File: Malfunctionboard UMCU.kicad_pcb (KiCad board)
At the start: 2 copper layers, 214 parts, among them J101 Conn_02x05_Odd_Even, J102 Conn_02x05_Odd_Even, J201 Conn_Coaxial, J202 Conn_Coaxial, J301 Conn_Coaxial, J302 Conn_Coaxial, J401 Conn_Coaxial, J402 Conn_Coaxial, J501 Conn_Coaxial, J502 Conn_Coaxial, J601 Conn_Coaxial, J602 Conn_Coaxial, J701 Conn_Coaxial, J702 Conn_Coaxial, J801 Conn_Coaxial, J802 Conn_Coaxial, J901 Conn_Coaxial, J902 Conn_Coaxial, Q101 NTR5103NT1G, Q102 RSC002P03T316, Q103 RSC002P03T316, Q104 NTR5103NT1G, Q201 NTR5103NT1G, Q202 NTR5103NT1G, Q301 NTR5103NT1G, Q302 NTR5103NT1G, Q401 NTR5103NT1G, Q402 NTR5103NT1G, Q501 NTR5103NT1G, Q502 NTR5103NT1G, Q601 NTR5103NT1G, Q602 NTR5103NT1G, Q701 NTR5103NT1G, Q702 NTR5103NT1G, Q801 NTR5103NT1G, Q802 NTR5103NT1G, Q901 NTR5103NT1G, Q902 NTR5103NT1G, U201 Opamp_Quad_Generic, U301 Opamp_Quad_Generic, U401 Opamp_Quad_Generic, U501 Opamp_Quad_Generic, U601 Opamp_Quad_Generic, U701 Opamp_Quad_Generic, U801 Opamp_Quad_Generic, U901 Opamp_Quad_Generic

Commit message: Made first pcb sketch, but is too wide
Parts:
- added J201: Conn_Coaxial, _Custom:Solder straight thin coax cable, F.Cu at (155.5, 185.1)
- added J201: Conn_Coaxial, _Custom:Solder straight thin coax cable, F.Cu at (89.5, 185.1)
- added J201: Conn_Coaxial, _Custom:Solder straight thin coax cable, F.Cu at (82.2, 185.1)
- added J201: Conn_Coaxial, _Custom:Solder straight thin coax cable, F.Cu at (74.9, 185.1)
- added J201: Conn_Coaxial, _Custom:Solder straight thin coax cable, F.Cu at (67.5, 185.1)
- added J201: Conn_Coaxial, _Custom:Solder straight thin coax cable, F.Cu at (60.2, 185.1)
- added J201: Conn_Coaxial, _Custom:Solder straight thin coax cable, F.Cu at (52.9, 185.1)
- added J201: Conn_Coaxial, _Custom:Solder straight thin coax cable, F.Cu at (45.5, 185.1)
- added J201: Conn_Coaxial, _Custom:Solder straight thin coax cable, F.Cu at (148.2, 185.1)
- added J201: Conn_Coaxial, _Custom:Solder straight thin coax cable, F.Cu at (140.8, 185.1)
- added J201: Conn_Coaxial, _Custom:Solder straight thin coax cable, F.Cu at (133.5, 185.1)
- added J201: Conn_Coaxial, _Custom:Solder straight thin coax cable, F.Cu at (126.2, 185.1)
- added J201: Conn_Coaxial, _Custom:Solder straight thin coax cable, F.Cu at (118.8, 185.1)
- added J201: Conn_Coaxial, _Custom:Solder straight thin coax cable, F.Cu at (111.5, 185.1)
- added J201: Conn_Coaxial, _Custom:Solder straight thin coax cable, F.Cu at (104.2, 185.1)
- added J201: Conn_Coaxial, _Custom:Solder straight thin coax cable, F.Cu at (96.9, 185.1)
- moved C203 272.1 mm to (89.2, 108.2), turned to 270 degrees
- moved R202 265.1 mm to (92.7, 105.0), turned to 270 degrees
- moved C204 263.4 mm to (89.2, 112.3), turned to 270 degrees
- moved R204 255.5 mm to (102.9, 124.0), turned to 90 degrees
- moved Q201 254.7 mm to (102.1, 115.6), turned to 270 degrees
- moved R205 253.8 mm to (97.5, 120.9), turned to 180 degrees
- moved R203 253.5 mm to (102.1, 120.9)
- moved Q202 252.7 mm to (97.5, 115.6), turned to 270 degrees
- moved L203 252.4 mm to (92.7, 111.3), turned to 90 degrees
- moved C201 251.3 mm to (110.5, 108.2), turned to 270 degrees
- moved L204 251.2 mm to (92.7, 118.9), turned to 90 degrees
- moved D201 250.9 mm to (102.9, 127.8), turned to 90 degrees
- moved R206 250.2 mm to (96.8, 124.0), turned to 90 degrees
- moved D202 249.6 mm to (96.8, 127.8), turned to 90 degrees
- moved C205 249.1 mm to (98.8, 118.6)
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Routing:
- net /Ref+: track 0.00 -> 45.7 mm, vias 0 -> 5
- net +12V: track 0.00 -> 44.2 mm, vias 0 -> 5
- net -5V: track 0.00 -> 41.9 mm, vias 0 -> 3
- net /Ref-: track 0.00 -> 40.5 mm, vias 0 -> 2
- net /sheet5DD8DCB3/LED_GND: track 0.00 -> 29.8 mm, vias 0 -> 2
- net Net-(D202-Pad1): track 0.00 -> 26.0 mm
- net Net-(D201-Pad1): track 0.00 -> 25.2 mm
- net Net-(C201-Pad2): track 0.00 -> 14.6 mm
- net /V_in: track 0.00 -> 14.2 mm
- net Net-(C203-Pad2): track 0.00 -> 14.2 mm
- net /sheet5DF3552C/Malf: track 0.00 -> 11.9 mm, vias 0 -> 1
- net /sheet5DF3552B/Malf: track 0.00 -> 11.9 mm, vias 0 -> 1
- net Net-(C204-Pad2): track 0.00 -> 6.98 mm
- net Net-(C202-Pad2): track 0.00 -> 6.98 mm
- net Net-(J202-Pad1): track 0.00 -> 6.50 mm
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- added copper zone on B.Cu, net GND
- added copper zone on F.Cu, net GND
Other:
- net class Default: via_dia 0.8 -> 0.6; via_drill 0.4 -> 0.25
- rule via_min_drill: 0.3 -> 0.25
- board text added: "Should be this far apart"

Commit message: Finished main pcb design. Todo: move decouple C's to backside, move logic at connectors to back, better mounting hole position
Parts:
- removed the C203 at (89.2, 108.2)
- removed the J201 at (155.5, 185.1)
- removed the J201 at (89.5, 185.1)
- removed the J201 at (82.2, 185.1)
- removed the J201 at (74.9, 185.1)
- removed the J201 at (67.5, 185.1)
- removed the J201 at (60.2, 185.1)
- removed the J201 at (52.9, 185.1)
- removed the J201 at (45.5, 185.1)
- removed the J201 at (106.9, 133.9)
- removed the J201 at (148.2, 185.1)
- removed the J201 at (140.8, 185.1)
- removed the J201 at (133.5, 185.1)
- removed the J201 at (126.2, 185.1)
- removed the J201 at (118.8, 185.1)
- removed the J201 at (111.5, 185.1)
- removed the J201 at (104.2, 185.1)
- removed the J201 at (96.9, 185.1)
- removed JP101, JP102: Jumper, Connector_PinHeader_2.54mm:PinHeader_1x02_P2.54mm_Vertical
- removed the R103 at (347.1, 40.5)
- removed the R201 at (106.9, 105.0)
- removed the R204 at (102.9, 124.0)
- added C204: 10n, Capacitor_SMD:C_0805_2012Metric, F.Cu at (103.6, 108.2)
- added D108: 5.4V, Diode_SMD:D_SOD-323, F.Cu at (81.8, 121.9)
- added D109: 12V, Diode_SMD:D_SOD-323, F.Cu at (86.4, 116.8)
- added H1: MH_Pad, MountingHole:MountingHole_3.2mm_M3, F.Cu at (88.6, 122.3)
- added H10: MH_Pad, MountingHole:MountingHole_3.2mm_M3, F.Cu at (148.1, 123.3)
- added H2: MH_Pad, MountingHole:MountingHole_3.2mm_M3, F.Cu at (88.6, 109.3)
- added H3: MH_Pad, MountingHole:MountingHole_3.2mm_M3, F.Cu at (208.5, 132.5)
- added H4: MH_Pad, MountingHole:MountingHole_3.2mm_M3, F.Cu at (68.0, 103.1)
- added H5: MH_Pad, MountingHole:MountingHole_3.2mm_M3, F.Cu at (208.3, 103.1)
- added H6: MH_Pad, MountingHole:MountingHole_3.2mm_M3, F.Cu at (68.0, 132.5)
- added H7: MH_Pad, MountingHole:MountingHole_3.2mm_M3, F.Cu at (71.9, 121.8)
- added H7: MH_Pad, MountingHole:MountingHole_3.2mm_M3, F.Cu at (71.9, 113.5)
- added H8: MH_Pad, MountingHole:MountingHole_3.2mm_M3, F.Cu at (177.6, 123.3)
- added H9: MH_Pad, MountingHole:MountingHole_3.2mm_M3, F.Cu at (118.4, 123.3)
- added J201: Conn_Coaxial, _Custom:Solder straight thin coax cable, F.Cu at (92.6, 129.9)
- added R101: 10k, Resistor_SMD:R_0805_2012Metric, F.Cu at (71.8, 115.4)
- added R203: 10k, Resistor_SMD:R_0805_2012Metric, B.Cu at (87.9, 130.7)
- added R205: 150R, Resistor_SMD:R_0805_2012Metric, F.Cu at (99.9, 105.5)
- C203: renamed from C205; moved to B.Cu
- C303: renamed from C305; moved to B.Cu
- C403: renamed from C405; moved to B.Cu
- C503: renamed from C505; moved to B.Cu
- C603: renamed from C605; moved to B.Cu
- C703: renamed from C705; moved to B.Cu
- C803: renamed from C805; moved to B.Cu
- C903: renamed from C905; moved to B.Cu
- D101, D107: value 15V -> 5.4V
- D103: value 5V -> 15V
- D104: value 12V -> 5V
- D105, D106: value 5.4V -> 15V
- Q101: value NTR5103NT1G -> RSC002P03T316
- Q103: value RSC002P03T316 -> NTR5103NT1G
- Q201, Q202, Q301, Q302, Q401, Q402, Q501, Q502, Q601, Q602, Q701, Q702, Q801, Q802, Q901, Q902, R206, R306, R406, R506, R606, R706, R806, R906, U201, U301, U401, U501, U601, U701, U801, U901: moved to B.Cu
- R102: value 10k -> 100k
- R201: renamed from R203; moved to B.Cu
- R204: renamed from R205; moved to B.Cu
- R301: renamed from R303; moved to B.Cu
- R303: renamed from R304; moved to B.Cu
- R304: renamed from R305; moved to B.Cu
- R401: renamed from R403; moved to B.Cu
- R403: renamed from R404; moved to B.Cu
- R404: renamed from R405; moved to B.Cu
- R501: renamed from R503; moved to B.Cu
- R503: renamed from R504; moved to B.Cu
- R504: renamed from R505; moved to B.Cu
- R601: renamed from R603; moved to B.Cu
- R603: renamed from R604; moved to B.Cu
- R604: renamed from R605; moved to B.Cu
- R701: renamed from R703; moved to B.Cu
- R703: renamed from R704; moved to B.Cu
- R704: renamed from R705; moved to B.Cu
- R801: renamed from R803; moved to B.Cu
- R803: renamed from R804; moved to B.Cu
- R804: renamed from R805; moved to B.Cu
- R901: renamed from R903; moved to B.Cu
- R903: renamed from R904; moved to B.Cu
- R904: renamed from R905; moved to B.Cu
- moved R303 317.3 mm to (102.7, 130.7), turned to 180 degrees
- moved D301 316.8 mm to (103.7, 131.6), turned to 90 degrees
- moved R302 312.7 mm to (107.4, 105.5), turned to 270 degrees
- moved C302 309.2 mm to (103.7, 114.7)
- moved Q302 307.4 mm to (113.3, 116.5), turned to 270 degrees
- moved R503 306.9 mm to (132.3, 130.7), turned to 180 degrees
- moved L301 306.6 mm to (107.4, 111.3), turned to 90 degrees
- moved R304 305.7 mm to (113.3, 121.8)
- moved R306 305.5 mm to (110.1, 130.7), turned to 180 degrees
- moved C303 305.4 mm to (112.1, 119.5), turned to 180 degrees
- moved R305 305.1 mm to (114.7, 105.5), turned to 270 degrees
- moved C501 304.1 mm to (133.3, 110.2)
- moved Q301 304.0 mm to (108.8, 116.5), turned to 270 degrees
- moved C301 303.5 mm to (103.7, 110.2)
- moved C305 303.4 mm to (118.4, 112.6), turned to 180 degrees
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- renumbered C103 to C102, C105 to C103, C107 to C104, C109 to C105, C111 to C106, C113 to C107, C115 to C108, C117 to C109, C119 to C110, C102 to C111, C104 to C112, C106 to C113, C108 to C114, C110 to C115, C112 to C116, C114 to C117, C116 to C118, C118 to C119, C204 to C205, C303 to C304, C304 to C305, C403 to C404, C404 to C405, C503 to C504, C504 to C505, C603 to C604, C604 to C605, C703 to C704, C704 to C705, C803 to C804, C804 to C805, C903 to C904, C904 to C905, R101 to R103, R301 to R302, R302 to R305, R401 to R402, R402 to R405, R501 to R502, R502 to R505, R601 to R602, R602 to R605, R701 to R702, R702 to R705, R801 to R802, R802 to R805, R901 to R902, R902 to R905
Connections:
- D101 pad 1: /Malf -> GND
- D101 pad 2: GND -> -5V
- D102 pad 1: Net-(D102-Pad1) -> +12V
- D103 pad 2: /V_in -> GND
- D104 pad 1: Net-(D103-Pad1) -> Net-(D104-Pad1)
- D104 pad 2: GND -> /V_in
- D105 pad 1: GND -> /Malf
- D105 pad 2: /Ref- -> GND
- D106 pad 1: GND -> Net-(D106-Pad1)
- D106 pad 2: /Ref+ -> GND
- D107 pad 1: Net-(D107-Pad1) -> GND
- D107 pad 2: GND -> /Ref-
- J101 pad 8: Net-(D102-Pad1) -> Net-(D106-Pad1)
- J102 pad 8: Net-(D107-Pad1) -> Net-(D103-Pad1)
- L203 pad 2: Net-(C203-Pad2) -> Net-(C204-Pad2)
- Q101 pad 1: /V_in -> /sheet5DD8DCB3/Malf_in
- Q101 pad 2: GND -> Net-(D106-Pad1)
- Q102 pad 2: Net-(D102-Pad1) -> Net-(D103-Pad1)
- Q102 pad 3: Net-(Q102-Pad3) -> Net-(Q101-Pad3)
- Q103 pad 1: /sheet5DD8DCB3/Malf_in -> Net-(Q103-Pad1)
- Q103 pad 2: Net-(D107-Pad1) -> GND
- Q103 pad 3: Net-(Q102-Pad3) -> /sheet5DD8DCB3/LED_GND
- Q104 pad 1: Net-(Q101-Pad3) -> /V_in
- Q104 pad 3: /sheet5DD8DCB3/LED_GND -> Net-(Q103-Pad1)
- Q201 pad 3: /sheet5DF3552B/Malf -> /sheet5DD8DCB3/Malf_in
- Q202 pad 2: /sheet5DF3552C/Malf -> /sheet5DD8DCB3/Malf
- Q301 pad 3: /sheet5DF270F1/Malf -> /sheet5DD8DCB3/Malf
- Q302 pad 2: /sheet5DF3552B/Malf -> /sheet5DE59C6C/Malf
- Q401 pad 3: /sheet5DF270F0/Malf -> /sheet5DE59C6C/Malf
- Q402 pad 2: /sheet5DF270F1/Malf -> /sheet5DF0CFC9/Malf
- Q501 pad 3: /sheet5DF0CFCA/Malf -> /sheet5DF0CFC9/Malf
- Q502 pad 2: /sheet5DF270F0/Malf -> /sheet5DF0CFCA/Malf
- Q601 pad 3: /sheet5DF0CFC9/Malf -> /sheet5DF0CFCA/Malf
- Q602 pad 2: /sheet5DF0CFCA/Malf -> /sheet5DF270F0/Malf
- Q701 pad 3: /sheet5DE59C6C/Malf -> /sheet5DF270F0/Malf
- Q702 pad 2: /sheet5DF0CFC9/Malf -> /sheet5DF270F1/Malf
- Q801 pad 3: /sheet5DD8DCB3/Malf -> /sheet5DF270F1/Malf
- Q802 pad 2: /sheet5DE59C6C/Malf -> /sheet5DF3552B/Malf
- Q901 pad 3: /sheet5DD8DCB3/Malf_in -> /sheet5DF3552B/Malf
- Q902 pad 2: /sheet5DD8DCB3/Malf -> /sheet5DF3552C/Malf
- R102 pad 2: /sheet5DD8DCB3/Malf_in -> Net-(Q103-Pad1)
- R202 pad 2: Net-(C203-Pad2) -> Net-(C201-Pad2)
- U201 pad 12: Net-(C203-Pad2) -> Net-(C204-Pad2)
- U201 pad 9: Net-(C203-Pad2) -> Net-(C204-Pad2)
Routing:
- net +12V: track 44.2 -> 363.9 mm, vias 5 -> 32
- net /Ref-: track 40.5 -> 277.8 mm, vias 2 -> 16
- net /Ref+: track 45.7 -> 261.3 mm, vias 5 -> 34
- net -5V: track 41.9 -> 209.5 mm, vias 3 -> 18
- net /V_in: track 14.2 -> 174.2 mm, vias 0 -> 3
- net /sheet5DD8DCB3/LED_GND: track 29.8 -> 182.1 mm, vias 2 -> 1
- net Net-(D801-Pad1): track 0.00 -> 31.7 mm, vias 0 -> 3
- net Net-(D501-Pad1): track 0.00 -> 31.7 mm, vias 0 -> 3
- net Net-(D901-Pad1): track 0.00 -> 31.7 mm, vias 0 -> 3
- net Net-(D601-Pad1): track 0.00 -> 31.7 mm, vias 0 -> 3
- net Net-(D301-Pad1): track 0.00 -> 31.7 mm, vias 0 -> 3
- net Net-(D401-Pad1): track 0.00 -> 31.7 mm, vias 0 -> 3
- net Net-(D701-Pad1): track 0.00 -> 31.7 mm, vias 0 -> 3
- net Net-(D902-Pad1): track 0.00 -> 31.4 mm, vias 0 -> 3
- net Net-(D702-Pad1): track 0.00 -> 31.4 mm, vias 0 -> 3
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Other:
- board outline added: 144.9 x 33.7 mm
- board text added: "Ch1"
- board text removed: "Should be this far apart"

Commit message: Finished v0.1
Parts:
- removed C101, C102, C103, C104, C105, C106, C107, C108, C109, C110, C111, C112, C113, C114, C115, C116, C117, C118, C119, C120: 10n, Capacitor_SMD:C_0805_2012Metric
- removed the D104 at (85.1, 119.6)
- removed the D105 at (74.2, 121.9)
- removed the D107 at (82.3, 118.5)
- removed H2, H4, H6, H7 (x2), H8, H9: MH_Pad, MountingHole:MountingHole_3.2mm_M3
- removed the Q104 at (79.2, 117.9)
- removed the R303 at (102.7, 130.7)
- removed the R403 at (117.5, 130.7)
- removed the R503 at (132.3, 130.7)
- removed the R603 at (147.1, 130.7)
- removed the R703 at (161.9, 130.7)
- removed the R803 at (176.7, 130.7)
- removed the R903 at (191.5, 130.7)
- added C201: 10n, Capacitor_SMD:C_0805_2012Metric, F.Cu at (88.8, 106.7)
- added C206: 10n, Capacitor_SMD:C_0805_2012Metric, B.Cu at (102.6, 105.3)
- added C207: 10n, Capacitor_SMD:C_0805_2012Metric, B.Cu at (91.8, 103.1)
- added C208: 10n, Capacitor_SMD:C_0805_2012Metric, B.Cu at (103.6, 108.5)
- added C209: 10n, Capacitor_SMD:C_0805_2012Metric, B.Cu at (97.2, 104.6)
- added C210: 10n, Capacitor_SMD:C_0805_2012Metric, B.Cu at (91.0, 119.0)
- added C212: 10n, Capacitor_SMD:C_0805_2012Metric, B.Cu at (93.5, 130.3)
- added C303: 10n, Capacitor_SMD:C_0805_2012Metric, B.Cu at (104.9, 114.8)
- added C306: 10n, Capacitor_SMD:C_0805_2012Metric, B.Cu at (117.4, 105.3)
- added C307: 10n, Capacitor_SMD:C_0805_2012Metric, B.Cu at (108.4, 104.6)
- added C308: 10n, Capacitor_SMD:C_0805_2012Metric, B.Cu at (118.4, 108.5)
- added C309: 10n, Capacitor_SMD:C_0805_2012Metric, B.Cu at (112.0, 104.6)
- added C310: 10n, Capacitor_SMD:C_0805_2012Metric, B.Cu at (103.7, 118.6)
- added C312: 10n, Capacitor_SMD:C_0805_2012Metric, B.Cu at (108.3, 130.3)
- added C403: 10n, Capacitor_SMD:C_0805_2012Metric, B.Cu at (119.7, 114.8)
- added C406: 10n, Capacitor_SMD:C_0805_2012Metric, B.Cu at (132.2, 105.3)
- added C407: 10n, Capacitor_SMD:C_0805_2012Metric, B.Cu at (123.2, 104.6)
- added C408: 10n, Capacitor_SMD:C_0805_2012Metric, B.Cu at (133.2, 108.5)
- added C409: 10n, Capacitor_SMD:C_0805_2012Metric, B.Cu at (126.8, 104.6)
- added C410: 10n, Capacitor_SMD:C_0805_2012Metric, B.Cu at (118.5, 118.6)
- added C412: 10n, Capacitor_SMD:C_0805_2012Metric, B.Cu at (123.1, 130.3)
- added C503: 10n, Capacitor_SMD:C_0805_2012Metric, B.Cu at (134.5, 114.8)
- added C506: 10n, Capacitor_SMD:C_0805_2012Metric, B.Cu at (147.0, 105.3)
- added C507: 10n, Capacitor_SMD:C_0805_2012Metric, B.Cu at (138.0, 104.6)
- added C508: 10n, Capacitor_SMD:C_0805_2012Metric, B.Cu at (148.0, 108.5)
- added C509: 10n, Capacitor_SMD:C_0805_2012Metric, B.Cu at (141.6, 104.6)
- added C510: 10n, Capacitor_SMD:C_0805_2012Metric, B.Cu at (133.3, 118.6)
- added C512: 10n, Capacitor_SMD:C_0805_2012Metric, B.Cu at (137.9, 130.3)
- added C603: 10n, Capacitor_SMD:C_0805_2012Metric, B.Cu at (149.3, 114.8)
- added C606: 10n, Capacitor_SMD:C_0805_2012Metric, B.Cu at (161.8, 105.3)
- added C607: 10n, Capacitor_SMD:C_0805_2012Metric, B.Cu at (152.8, 104.6)
- added C608: 10n, Capacitor_SMD:C_0805_2012Metric, B.Cu at (162.8, 108.5)
- added C609: 10n, Capacitor_SMD:C_0805_2012Metric, B.Cu at (156.4, 104.6)
- added C610: 10n, Capacitor_SMD:C_0805_2012Metric, B.Cu at (148.1, 118.6)
- added C612: 10n, Capacitor_SMD:C_0805_2012Metric, B.Cu at (152.7, 130.3)
- added C703: 10n, Capacitor_SMD:C_0805_2012Metric, B.Cu at (164.1, 114.8)
- added C706: 10n, Capacitor_SMD:C_0805_2012Metric, B.Cu at (176.6, 105.3)
- added C707: 10n, Capacitor_SMD:C_0805_2012Metric, B.Cu at (167.6, 104.6)
- added C708: 10n, Capacitor_SMD:C_0805_2012Metric, B.Cu at (177.6, 108.5)
- added C709: 10n, Capacitor_SMD:C_0805_2012Metric, B.Cu at (171.2, 104.6)
- added C710: 10n, Capacitor_SMD:C_0805_2012Metric, B.Cu at (162.9, 118.6)
- added C712: 10n, Capacitor_SMD:C_0805_2012Metric, B.Cu at (167.5, 130.3)
- added C803: 10n, Capacitor_SMD:C_0805_2012Metric, B.Cu at (178.9, 114.8)
- added C806: 10n, Capacitor_SMD:C_0805_2012Metric, B.Cu at (191.4, 105.3)
- added C807: 10n, Capacitor_SMD:C_0805_2012Metric, B.Cu at (182.4, 104.6)
- added C808: 10n, Capacitor_SMD:C_0805_2012Metric, B.Cu at (192.4, 108.4)
- added C809: 10n, Capacitor_SMD:C_0805_2012Metric, B.Cu at (186.0, 104.6)
- added C810: 10n, Capacitor_SMD:C_0805_2012Metric, B.Cu at (177.7, 118.6)
- added C812: 10n, Capacitor_SMD:C_0805_2012Metric, B.Cu at (182.3, 130.3)
- added C903: 10n, Capacitor_SMD:C_0805_2012Metric, B.Cu at (193.7, 114.8)
- added C906: 10n, Capacitor_SMD:C_0805_2012Metric, B.Cu at (205.0, 105.9)
- added C907: 10n, Capacitor_SMD:C_0805_2012Metric, B.Cu at (197.2, 104.6)
- added C908: 10n, Capacitor_SMD:C_0805_2012Metric, B.Cu at (205.7, 108.0)
- added C909: 10n, Capacitor_SMD:C_0805_2012Metric, B.Cu at (200.8, 104.6)
- added C910: 10n, Capacitor_SMD:C_0805_2012Metric, B.Cu at (192.5, 118.6)
- added C912: 10n, Capacitor_SMD:C_0805_2012Metric, B.Cu at (197.1, 130.3)
- added D101: 15V, Diode_SMD:D_SOD-323, F.Cu at (76.5, 120.4)
- added D103: 5V, Diode_SMD:D_SOD-323, F.Cu at (81.9, 115.8)
- added D106: 5.4V, Diode_SMD:D_SOD-323, F.Cu at (80.4, 120.4)
- added H101: MH_Pad, MountingHole:MountingHole_3.2mm_M3, F.Cu at (86.9, 117.9)
- added H107: MH_Pad, MountingHole:MountingHole_3.2mm_M3, F.Cu at (85.9, 103.1)
- added H108: MH_Pad, MountingHole:MountingHole_3.2mm_M3, F.Cu at (85.6, 131.6)
- added Q103: RSC002P03T316, Package_TO_SOT_SMD:SOT-23, B.Cu at (79.1, 117.9)
- added R304: 10k, Resistor_SMD:R_0805_2012Metric, B.Cu at (104.7, 132.6)
- added R404: 10k, Resistor_SMD:R_0805_2012Metric, B.Cu at (119.4, 132.6)
- added R504: 10k, Resistor_SMD:R_0805_2012Metric, B.Cu at (134.2, 132.6)
- added R604: 10k, Resistor_SMD:R_0805_2012Metric, B.Cu at (149.0, 132.6)
- added R704: 10k, Resistor_SMD:R_0805_2012Metric, B.Cu at (163.8, 132.6)
- added R804: 10k, Resistor_SMD:R_0805_2012Metric, B.Cu at (178.6, 132.6)
- added R904: 10k, Resistor_SMD:R_0805_2012Metric, B.Cu at (193.4, 132.6)
- added SYM101: SYM_Magnet_Small, _Custom:UMC_logo_small, B.Cu at (114.0, 125.6)
- C202: renamed from C201; moved to B.Cu
- C203: renamed from C202; moved to B.Cu
- C204, C205, C302, C304, C305, C402, C404, C405, C502, C504, C505, C602, C604, C605, C702, C704, C705, C802, C804, C805, C902, C904, C905, Q102: moved to B.Cu
- D102: renamed from D106; moved to B.Cu
- D109: renamed from D103; moved to B.Cu
- Q101: value RSC002P03T316 -> NTR5103NT1G; moved to B.Cu
- Q104: renamed from Q103; moved to B.Cu
- R101: renamed from R103; moved to B.Cu
- R102: renamed from R101; moved to B.Cu
- R103: renamed from R102; moved to B.Cu
- U201, U301, U401, U501, U601, U701, U801, U901: value Opamp_Quad_Generic -> LM339PW
- moved R101 163.4 mm to (205.7, 118.7), turned to 270 degrees
- moved H104 17.8 mm to (71.4, 117.9)
- moved R102 14.9 mm to (86.5, 113.3), turned to 180 degrees
- moved D107 9.43 mm to (75.2, 113.4), turned to 0 degrees
- moved D108 8.54 mm to (82.5, 113.4), turned to 180 degrees
- moved D104 7.94 mm to (78.5, 115.8), turned to 180 degrees
- moved D109 7.79 mm to (75.3, 114.2)
- moved Q101 7.60 mm to (76.5, 121.7), turned to 90 degrees
- moved R103 6.03 mm to (75.7, 117.9), turned to 270 degrees
- moved D105 4.98 mm to (77.6, 118.1), turned to 180 degrees
- moved C901 4.83 mm to (192.4, 105.4), turned to 90 degrees
- moved C301 4.83 mm to (103.6, 105.4), turned to 90 degrees
- moved C401 4.83 mm to (118.4, 105.4), turned to 90 degrees
- moved C501 4.83 mm to (133.2, 105.4), turned to 90 degrees
- moved C601 4.83 mm to (148.0, 105.4), turned to 90 degrees
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- renumbered C203 to C211, C303 to C311, C403 to C411, C503 to C511, C603 to C611, C703 to C711, C803 to C811, C903 to C911, D109 to D104, D101 to D105, D102 to D107, H5 to H102, H1 to H104, H3 to H105, H10 to H106, R202 to R201, R205 to R202, R201 to R203, R203 to R204, R204 to R205, R302 to R301, R305 to R302, R301 to R303, R304 to R305, R402 to R401, R405 to R402, R401 to R403, R404 to R405, R502 to R501, R505 to R502, R501 to R503, R504 to R505, R602 to R601, R605 to R602, R601 to R603, R604 to R605, R702 to R701, R705 to R702, R701 to R703, R704 to R705, R802 to R801, R805 to R802, R801 to R803, R804 to R805, R902 to R901, R905 to R902, R901 to R903, R904 to R905
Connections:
- C301 pad 2: Net-(C301-Pad2) -> /V_in
- C401 pad 2: Net-(C401-Pad2) -> /V_in
- C501 pad 2: Net-(C501-Pad2) -> /V_in
- C601 pad 2: Net-(C601-Pad2) -> /V_in
- C701 pad 2: Net-(C701-Pad2) -> /V_in
- C801 pad 2: Net-(C801-Pad2) -> /V_in
- C901 pad 2: Net-(C901-Pad2) -> /V_in
- D102 pad 1: Net-(D106-Pad1) -> Net-(D102-Pad1)
- D109 pad 1: Net-(D103-Pad1) (its old number) -> Net-(D109-Pad1)
- J101 pad 8: Net-(D106-Pad1) -> Net-(D102-Pad1)
- J102 pad 8: Net-(D103-Pad1) (its old number) -> Net-(D109-Pad1)
- L301 pad 1: Net-(C302-Pad2) -> Net-(C303-Pad2)
- L301 pad 2: Net-(C301-Pad2) -> Net-(C302-Pad2)
- L302 pad 2: Net-(C302-Pad2) -> Net-(C303-Pad2)
- L401 pad 1: Net-(C402-Pad2) -> Net-(C403-Pad2)
- L401 pad 2: Net-(C401-Pad2) -> Net-(C402-Pad2)
- L402 pad 2: Net-(C402-Pad2) -> Net-(C403-Pad2)
- L501 pad 1: Net-(C502-Pad2) -> Net-(C503-Pad2)
- L501 pad 2: Net-(C501-Pad2) -> Net-(C502-Pad2)
- L502 pad 2: Net-(C502-Pad2) -> Net-(C503-Pad2)
- L601 pad 1: Net-(C602-Pad2) -> Net-(C603-Pad2)
- L601 pad 2: Net-(C601-Pad2) -> Net-(C602-Pad2)
- L602 pad 2: Net-(C602-Pad2) -> Net-(C603-Pad2)
- L701 pad 1: Net-(C702-Pad2) -> Net-(C703-Pad2)
- L701 pad 2: Net-(C701-Pad2) -> Net-(C702-Pad2)
- L702 pad 2: Net-(C702-Pad2) -> Net-(C703-Pad2)
- L801 pad 1: Net-(C802-Pad2) -> Net-(C803-Pad2)
- L801 pad 2: Net-(C801-Pad2) -> Net-(C802-Pad2)
- L802 pad 2: Net-(C802-Pad2) -> Net-(C803-Pad2)
- L901 pad 1: Net-(C902-Pad2) -> Net-(C903-Pad2)
- L901 pad 2: Net-(C901-Pad2) -> Net-(C902-Pad2)
- L902 pad 2: Net-(C902-Pad2) -> Net-(C903-Pad2)
- Q101 pad 1: /sheet5DD8DCB3/Malf_in -> /V_in
- Q101 pad 2: Net-(D106-Pad1) -> GND
- Q102 pad 2: Net-(D103-Pad1) (its old number) -> Net-(D102-Pad1)
- Q102 pad 3: Net-(Q101-Pad3) -> Net-(Q102-Pad3)
- Q104 pad 1: Net-(Q103-Pad1) -> Net-(Q101-Pad3)
- R103 pad 2: Net-(Q103-Pad1) -> Net-(Q101-Pad3)
- R301 pad 2: Net-(C301-Pad2) -> Net-(C302-Pad2)
- R401 pad 2: Net-(C401-Pad2) -> Net-(C402-Pad2)
- R501 pad 2: Net-(C501-Pad2) -> Net-(C502-Pad2)
- R601 pad 2: Net-(C601-Pad2) -> Net-(C602-Pad2)
- R701 pad 2: Net-(C701-Pad2) -> Net-(C702-Pad2)
- R801 pad 2: Net-(C801-Pad2) -> Net-(C802-Pad2)
- R901 pad 2: Net-(C901-Pad2) -> Net-(C902-Pad2)
- U301 pad 2: Net-(C301-Pad2) -> Net-(C302-Pad2)
- U301 pad 5: Net-(C301-Pad2) -> Net-(C302-Pad2)
- U401 pad 2: Net-(C401-Pad2) -> Net-(C402-Pad2)
- U401 pad 5: Net-(C401-Pad2) -> Net-(C402-Pad2)
- U501 pad 2: Net-(C501-Pad2) -> Net-(C502-Pad2)
- U501 pad 5: Net-(C501-Pad2) -> Net-(C502-Pad2)
- U601 pad 2: Net-(C601-Pad2) -> Net-(C602-Pad2)
- U601 pad 5: Net-(C601-Pad2) -> Net-(C602-Pad2)
- U701 pad 2: Net-(C701-Pad2) -> Net-(C702-Pad2)
- U701 pad 5: Net-(C701-Pad2) -> Net-(C702-Pad2)
- U801 pad 2: Net-(C801-Pad2) -> Net-(C802-Pad2)
- U801 pad 5: Net-(C801-Pad2) -> Net-(C802-Pad2)
- U901 pad 2: Net-(C901-Pad2) -> Net-(C902-Pad2)
- U901 pad 5: Net-(C901-Pad2) -> Net-(C902-Pad2)
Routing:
- net /sheet5DD8DCB3/LED_GND: track 182.1 -> 142.3 mm, vias 1 -> 2
- net +12V: track 363.9 -> 381.6 mm, vias 32 -> 37
- net Net-(D109-Pad1): track 0.00 -> 15.9 mm, vias 0 -> 1
- net Net-(Q103-Pad1): track 14.5 -> 0.00 mm, vias 2 -> 0
- net Net-(D106-Pad1): track 14.1 -> 0.00 mm
- net Net-(C701-Pad2): track 11.4 -> 0.00 mm, vias 1 -> 0
- net Net-(C401-Pad2): track 11.4 -> 0.00 mm, vias 1 -> 0
- net Net-(C601-Pad2): track 11.4 -> 0.00 mm, vias 1 -> 0
- net Net-(C301-Pad2): track 11.4 -> 0.00 mm, vias 1 -> 0
- net Net-(C801-Pad2): track 11.4 -> 0.00 mm, vias 1 -> 0
- net Net-(C901-Pad2): track 11.4 -> 0.00 mm, vias 1 -> 0
- net Net-(C501-Pad2): track 11.4 -> 0.00 mm, vias 1 -> 0
- net /Ref+: track 261.3 -> 272.3 mm, vias 34 -> 33
- net Net-(D103-Pad1) (its old number): track 10.8 -> 0.00 mm
- net /Ref-: track 277.8 -> 287.4 mm, vias 16 -> 18
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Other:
- board size 144.9 x 33.7 mm -> 141.4 x 32.7 mm
- board text added: "+12V -5V GND Malf Ref+"
- board text added: "11/2019 v0.1"
- board text added: "Ch10"
- board text added: "Ch11"
- board text added: "Ch12"
- board text added: "Ch13"
- board text added: "Ch14"
- board text added: "Ch15"
- board text added: "Ch16"
- board text added: "Ch2"
- board text added: "Ch3"
- board text added: "Ch4"
- board text added: "Ch5"
- board text added: "Ch6"
- board text added: "Ch7"
- board text added: "Ch8"
- board text added: "Ch9"
- board text added: "DW"
- board text added: "Det Det GND MD Ref-"
- board text added: "In/Out"
- board text added: "Malf/MD jumper on last board OUT"
- board text added: "Malfunctionboard"
- board text added: "Malfunctionboard v0.1"
- board text added: "Ref+ Malf GND -5V +12V"
- board text added: "Ref- MD GND Det Det"

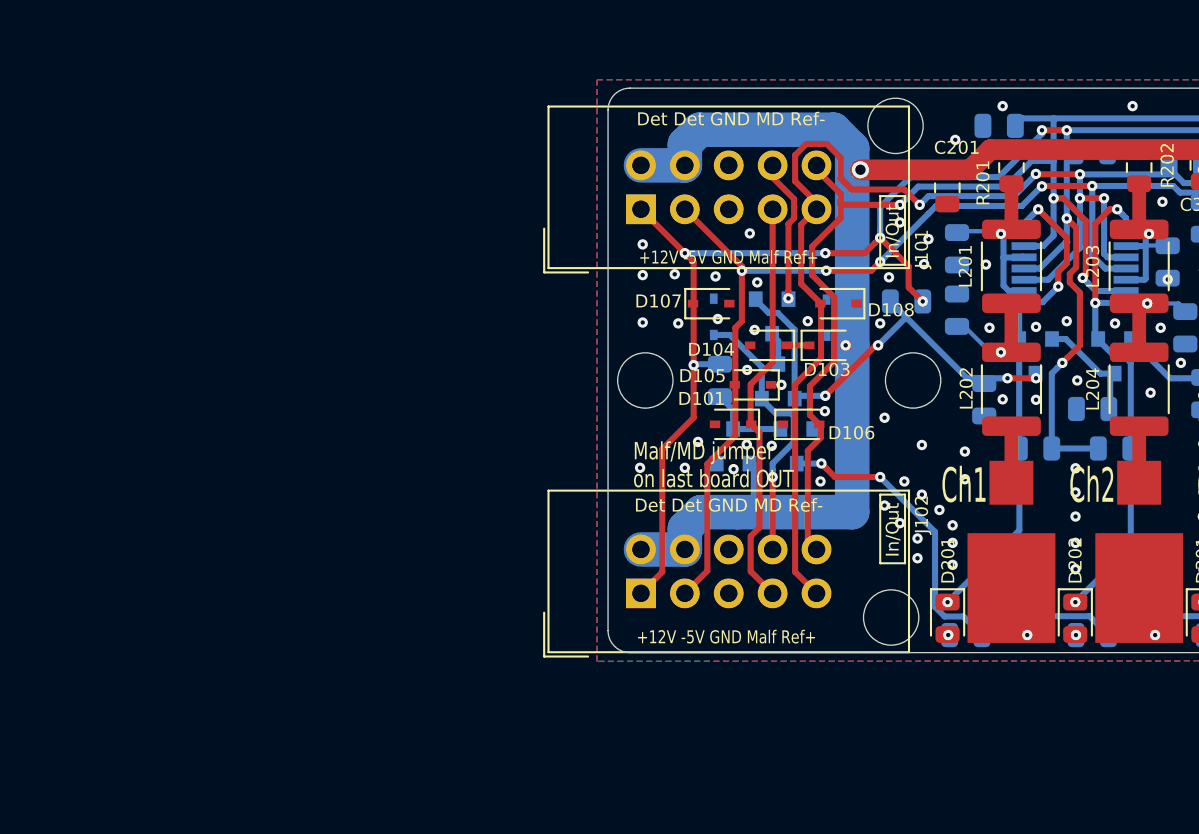
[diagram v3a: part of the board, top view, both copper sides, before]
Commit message: Changed: started changing circuit between connectors
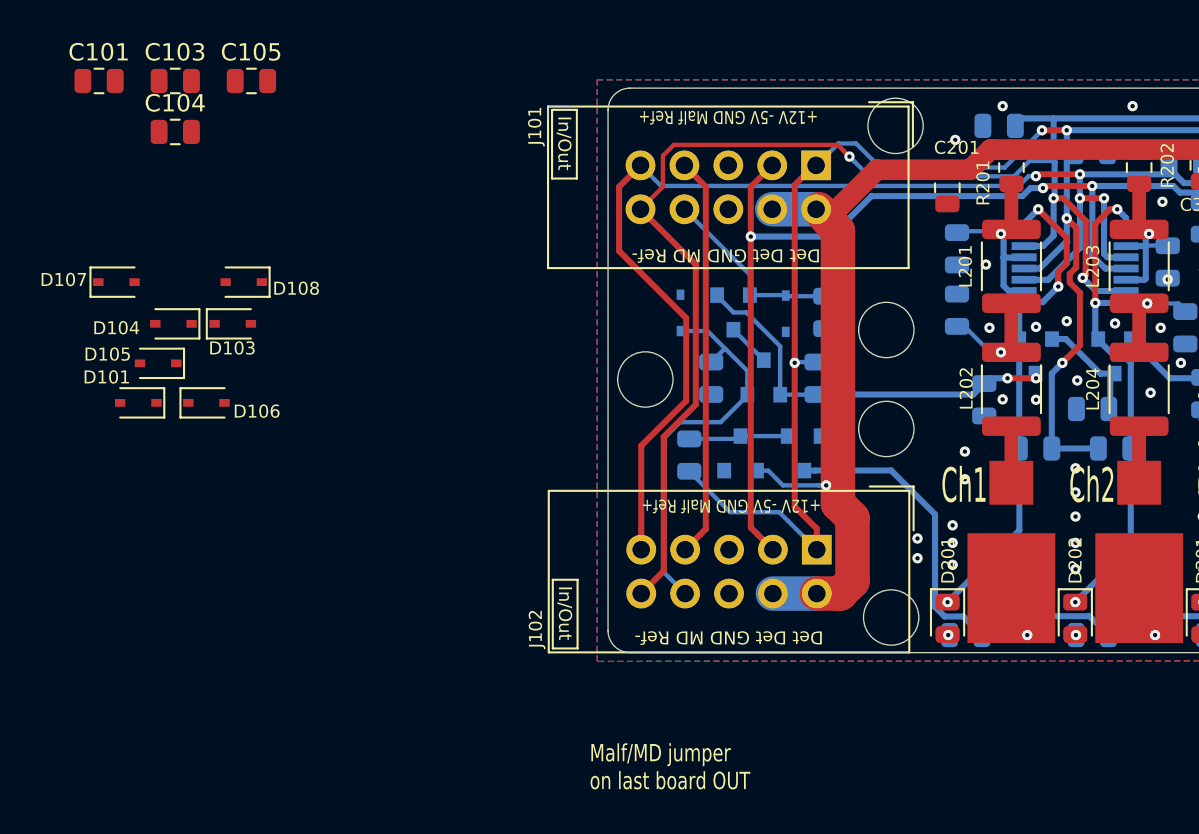
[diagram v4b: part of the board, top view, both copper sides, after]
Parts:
- added C101: 10n, Capacitor_SMD:C_0805_2012Metric, F.Cu at (39.8, 100.5)
- added C102: 10n, Capacitor_SMD:C_0805_2012Metric, B.Cu at (81.8, 113.9)
- added C103: 10n, Capacitor_SMD:C_0805_2012Metric, F.Cu at (44.2, 100.5)
- added C104: 10n, Capacitor_SMD:C_0805_2012Metric, F.Cu at (44.2, 103.5)
- added C105: 10n, Capacitor_SMD:C_0805_2012Metric, F.Cu at (48.6, 100.5)
- added C106: 10n, Capacitor_SMD:C_0805_2012Metric, B.Cu at (75.2, 117.7)
- added H101: MH_Pad, MountingHole:MountingHole_3.2mm_M3, F.Cu at (85.3, 120.7)
- moved D103 34.4 mm to (47.5, 114.6)
- moved D106 34.4 mm to (46.0, 119.2)
- moved D104 34.4 mm to (44.1, 114.6)
- moved D101 34.4 mm to (42.0, 119.2)
- moved D105 34.4 mm to (43.2, 116.9)
- moved D107 34.4 mm to (40.8, 112.2)
- moved D108 34.4 mm to (48.1, 112.2)
- moved J102 10.5 mm to (81.3, 127.6), turned to 270 degrees
- moved J101 10.4 mm to (81.3, 105.4), turned to 270 degrees
- moved R102 6.85 mm to (81.3, 117.7), turned to 270 degrees
- moved R103 4.67 mm to (73.9, 122.2), turned to 90 degrees
- moved H101 3.31 mm to (85.3, 114.9)
- moved D102 2.37 mm to (79.5, 114.0)
- moved Q102 2.25 mm to (76.5, 113.9)
- moved D109 1.94 mm to (73.4, 113.9)
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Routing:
- net /V_in: track 172.4 -> 157.7 mm, vias 2 -> 1
- net /Ref-: track 287.4 -> 301.0 mm
- net +12V: track 381.6 -> 374.8 mm, vias 37 -> 33
- net Net-(C106-Pad2): track 15.9 -> 22.7 mm, vias 1 -> 0
- net /Ref+: track 272.3 -> 276.5 mm, vias 33 -> 32
- net /sheet5DD8DCB3/Malf_in: track 26.5 -> 22.9 mm, vias 4 -> 2
- net Net-(C102-Pad2): track 8.34 -> 11.7 mm, vias 1 -> 0
- net -5V: track 212.5 -> 209.5 mm, vias 19 -> 17
- net Net-(D103-Pad1): track 1.33 -> 0.00 mm
- net Net-(Q101-Pad3): track 4.92 -> 5.77 mm
- net Net-(Q102-Pad3): track 1.80 -> 2.42 mm
- net /sheet5DD8DCB3/LED_GND: vias 2 -> 0
- net GND: vias 334 -> 301
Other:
- board size 141.4 x 32.7 mm -> 144.9 x 32.7 mm
